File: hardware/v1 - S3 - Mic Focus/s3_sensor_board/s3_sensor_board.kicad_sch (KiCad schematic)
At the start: 10 parts, among them J101 Conn_01x02, J102 Conn_01x02, J103 Conn_01x02, J104 Conn_01x02

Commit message: WIP
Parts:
- removed J102, J103, J104: Conn_01x02, Connector_Phoenix_MSTB:PhoenixContact_MSTBA_2,5_2-G-5,08_1x02_P5.08mm_Horizontal, symbol Connector_Generic:Conn_01x02
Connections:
- net Vbus1_in renamed Microprocessor/VIN
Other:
- removed sheet Power Measurement
- added sheet Battery (mpu_battery.kicad_sch)
- moved on the sheet: J101

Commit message: WIP
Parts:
- added D101: D USB, Diode_SMD:D_SOD-123, symbol Device:D_Small
- added J102: PWR, Connector_PinHeader_2.54mm:PinHeader_1x03_P2.54mm_Vertical, symbol Connector_Generic:Conn_01x03
- added R101: 500k, Resistor_SMD:R_0603_1608Metric, symbol Device:R_Small
- added R102: 100k, Resistor_SMD:R_0603_1608Metric, symbol Device:R_Small
- J101: footprint Connector_Phoenix_MSTB:PhoenixContact_MSTBA_2,5_2-G-5,08_1x02_P5.08mm_Horizontal -> Connector_PinHeader_2.54mm:PinHeader_1x02_P2.54mm_Vertical
- renumbered R101 to R103, R102 to R104
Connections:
- net +3.3V: now also J102.2 (Pin_2)
- net GND: now also J102.1 (Pin_1), R102.2
- net Microprocessor/VIN renamed TPS56425X Regulator/Vin
- net TPS56425X Regulator/Vin: now also D101.1 (K), R101.1
- new net Microprocessor/V_usb: D101.2 (A)
- new net Microprocessor/Vin_DIV: R101.2, R102.1
- new net TPS56425X Regulator/PWR_GD: J102.3 (Pin_3)
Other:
- removed sheet Battery
- removed sheet Power
- added sheet PDM Interconnections (pdm_connections.kicad_sch)
- added sheet PDM Mics (pdm_mics.kicad_sch)
- added sheet TPS56425X Regulator (TPS56425X.kicad_sch)
- sheet Microprocessor ports: added PDM_CLK, PDM_D0, PDM_D1, PDM_D2, PDM_D3, V_usb, Vin_DIV; removed SPI_CIPO, SPI_COPI, SPI_CS1, SPI_SCK, VIN
- note added: "Goals: - ESP32-S3 based - Support for a 12V LiFePo4 solar system in power and power measurement - Optional support for a 1S LiPo cell with an off-board - Support for an optional load cell measurement - Support for a micro-SD card for logging - Support for 8 channels of PDM microphones - Support for touch sensors"
- note added: "Voltage divider to measure Vin Intended to keep the 3V to 15V range in the linear region of the ESP32-S3's ADC"
- note removed: "Goals: - ESP32-C1 based - Support for a 24V LiFePo4 solar system in power and power measurement - Support on board for 0-2 power measurement channels - Support for an optional load cell measurement - Support for a micro-SD card for logging Secondary - Optional support for an LCD - Breakout remaining GPIO / comms channels"
- note removed: "I2C Addresses: - 0x2A - NAU7802 Load Cell Amplifier - 0x44 - SHT4x - 0x46 - INA237 - 1 0x45 on prototype board after modification - 0x47 - INA237 - 2"
- moved on the sheet: R103, R104

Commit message: WIP
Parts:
- added J103: EXP, Connector_IDC:IDC-Header_2x05_P2.54mm_Vertical, symbol Connector_Generic:Conn_02x05_Odd_Even
- H101, H102, H103, H104: footprint MountingHole:MountingHole_3.2mm_M3_DIN965_Pad -> MountingHole:MountingHole_2.2mm_M2_DIN965_Pad
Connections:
- net GND: now also J103.1 (Pin_1)
- net Load Cell Sensor/SCK renamed I2C_SCL
- net I2C_SCL: now also J103.8 (Pin_8)
- net Load Cell Sensor/SDA renamed I2C_SDA
- net I2C_SDA: now also J103.9 (Pin_9)
- new net +3V3: J103.2 (Pin_2)
- new net INT: J103.10 (Pin_10)
- new net PDM_CLK: J103.3 (Pin_3)
- new net PDM_D0: J103.4 (Pin_4)
- new net PDM_D1: J103.5 (Pin_5)
- new net PDM_D2: J103.6 (Pin_6)
- new net PDM_D3: J103.7 (Pin_7)
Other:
- removed sheet Load Cell Sensor
- removed sheet PDM Interconnections
- removed sheet PDM Mics
- moved on the sheet: R103, R104

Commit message: Layout, starting DRC
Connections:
- net +3V3 is gone; now on net +3.3V: J103.2 (Pin_2)
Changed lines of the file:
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@@
 	)
 	(symbol
-		(lib_id "power:+3V3")
+		(lib_name "+3.3V_1")
+		(lib_id "power:+3.3V")
 		(at 161.29 110.49 0)
 		(unit 1)
@@
 			)
 		)
-		(property "Value" "+3V3"
+		(property "Value" "+3.3V"
 			(at 161.29 105.41 0)
 			(show_name no)
@@
 			)
 		)
-		(property "Description" "Power symbol creates a global label with name \"+3V3\""
+		(property "Description" "Power symbol creates a global label with name \"+3.3V\""
 			(at 161.29 110.49 0)
 			(hide yes)

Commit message: S3 WIP - Initial submission
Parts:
- removed H103, H104: MountingHole_Pad, MountingHole:MountingHole_2.2mm_M2_DIN965_Pad, symbol Mechanical:MountingHole_Pad

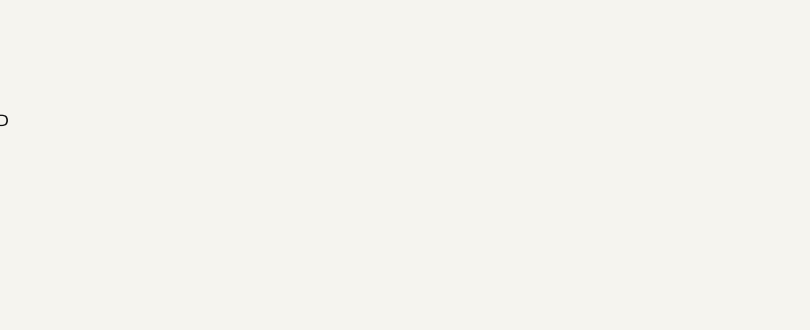
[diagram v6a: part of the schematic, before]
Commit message: Standoff move, silkscreen work
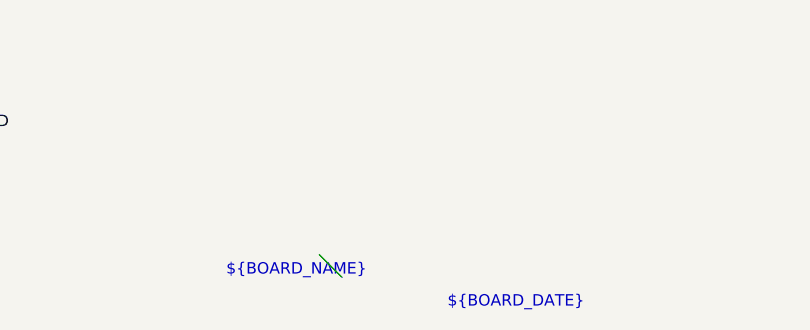
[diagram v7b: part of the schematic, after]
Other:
- note added: "${BOARD_DATE}"
- note added: "${BOARD_NAME}"
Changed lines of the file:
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@@
 	(generator_version "10.0")
 	(paper "A4")
+	(text "${BOARD_DATE}"
+		(exclude_from_sim no)
+		(at 213.614 193.294 0)
+		(effects
+			(font
+				(size 1.27 1.27)
+			)
+		)
+	)
 	(text "Goals:\n- ESP32-S3 based\n- Support for a 12V LiFePo4 solar system in power and power measurement\n- Optional support for a 1S LiPo cell with an off-board \n- Support for an optional load cell measurement\n- Support for a micro-SD card for logging\n- Support for 8 channels of PDM microphones\n- Support for touch sensors"
 		(exclude_from_sim no)
@@
 			)
 			(justify left bottom)
+		)
+	)
+	(text "${BOARD_NAME}"
+		(exclude_from_sim no)
+		(at 189.23 189.738 0)
+		(effects
+			(font
+				(size 1.27 1.27)
+			)
 		)
 	)
@@
 		(color 0 0 0 0)
 	)
+	(bus_entry
+		(at 191.77 187.96)
+		(size 2.54 2.54)
+		(stroke
+			(width 0)
+			(type default)
+		)
+	)
 	(wire
